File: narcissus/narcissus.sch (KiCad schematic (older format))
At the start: 71 parts, among them J1 NEIGHBOR1, J2 NEIGHBOR2, U1 PCA9698, U2 PCA9698, U3 AP2553W6-7, U4 74HC4051

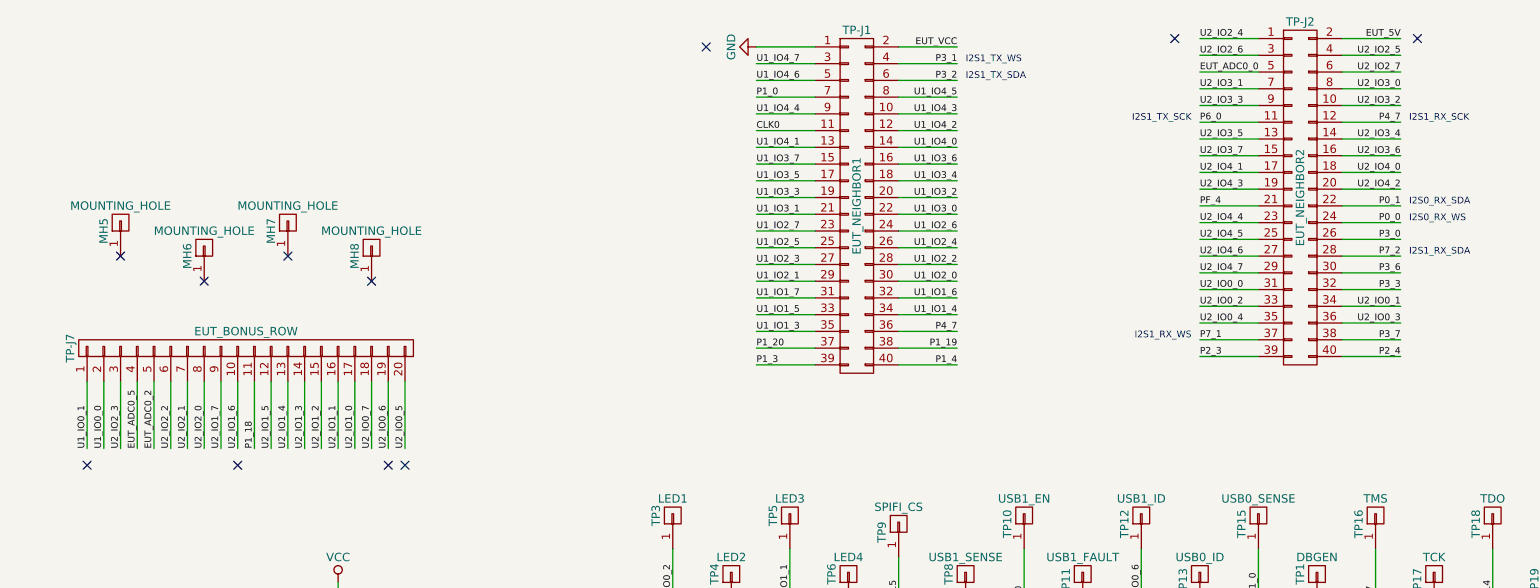
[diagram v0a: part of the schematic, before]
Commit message: Narcissus: corrected U4 pin 7 power supply connection
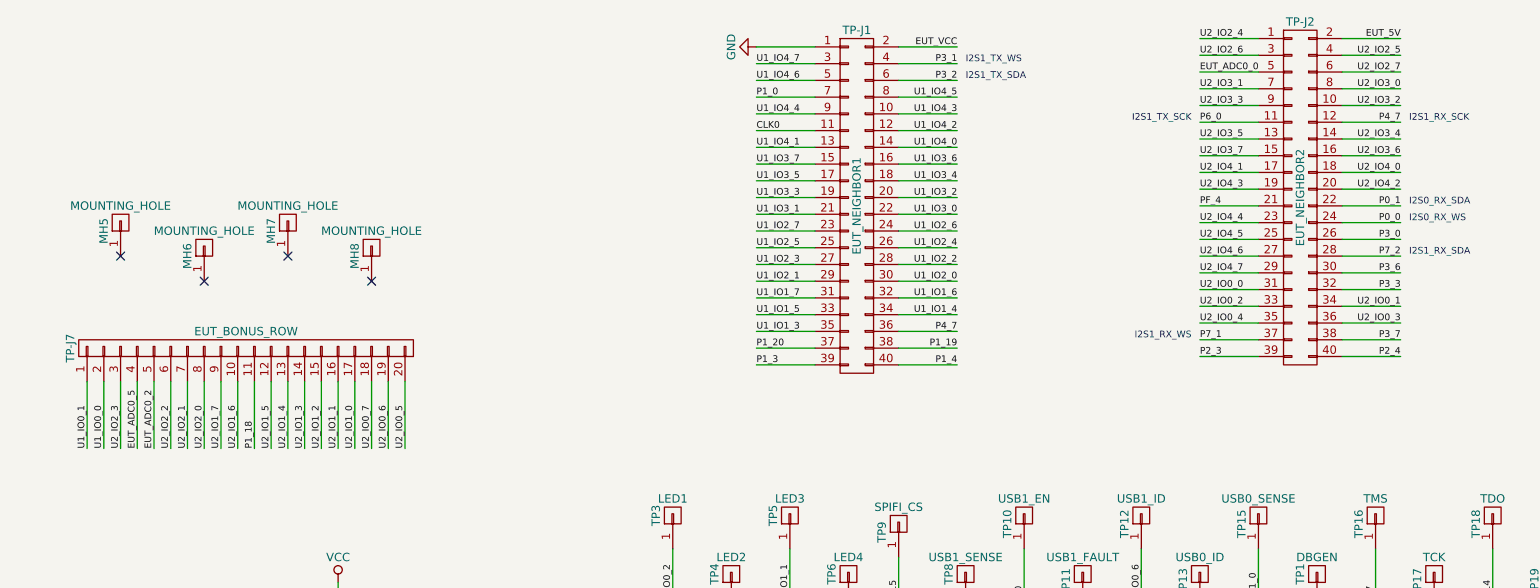
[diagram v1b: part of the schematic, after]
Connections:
- no-connect marks 48 -> 41
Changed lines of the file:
@@
 Sheet 1 1
 Title "Narcissus"
-Date "2018-06-28"
+Date "2018-07-24"
 Rev ""
 Comp "Copyright 2018 Great Scott Gadgets"
@@
 $EndComp
 $Comp
-L GND #PWR032
+L GND #PWR031
 U 1 1 5B3A7C8D
 P 3500 9300
-F 0 "#PWR032" H 3500 9050 50  0001 C CNN
+F 0 "#PWR031" H 3500 9050 50  0001 C CNN
 F 1 "GND" H 3500 9150 50  0000 C CNN
 F 2 "" H 3500 9300 50  0001 C CNN
@@
 $EndComp
 $Comp
-L VCC #PWR034
+L VCC #PWR032
 U 1 1 5B3A8A67
 P 5500 9300
-F 0 "#PWR034" H 5500 9150 50  0001 C CNN
+F 0 "#PWR032" H 5500 9150 50  0001 C CNN
 F 1 "VCC" H 5500 9450 50  0000 C CNN
 F 2 "" H 5500 9300 60  0000 C CNN
@@
 $EndComp
 $Comp
-L GND #PWR035
+L GND #PWR033
 U 1 1 5B3A8BCE
 P 5500 10000
-F 0 "#PWR035" H 5500 9750 50  0001 C CNN
+F 0 "#PWR033" H 5500 9750 50  0001 C CNN
 F 1 "GND" H 5500 9850 50  0000 C CNN
 F 2 "" H 5500 10000 50  0001 C CNN
@@
 $EndComp
 $Comp
-L VCC #PWR036
+L VCC #PWR034
 U 1 1 5B3A9F00
 P 8500 9300
-F 0 "#PWR036" H 8500 9150 50  0001 C CNN
+F 0 "#PWR034" H 8500 9150 50  0001 C CNN
 F 1 "VCC" H 8500 9450 50  0000 C CNN
 F 2 "" H 8500 9300 60  0000 C CNN
@@
 $EndComp
 $Comp
-L GND #PWR037
+L GND #PWR035
 U 1 1 5B3A9F06
 P 8500 10000
-F 0 "#PWR037" H 8500 9750 50  0001 C CNN
+F 0 "#PWR035" H 8500 9750 50  0001 C CNN
 F 1 "GND" H 8500 9850 50  0000 C CNN
 F 2 "" H 8500 10000 50  0001 C CNN
@@
 $EndComp
 $Comp
-L GND #PWR038
+L GND #PWR036
 U 1 1 5B3ACAB2
 P 1300 7850
-F 0 "#PWR038" H 1300 7600 50  0001 C CNN
+F 0 "#PWR036" H 1300 7600 50  0001 C CNN
 F 1 "GND" H 1300 7700 50  0000 C CNN
 F 2 "" H 1300 7850 50  0001 C CNN
@@
 $EndComp
 $Comp
-L GND #PWR039
+L GND #PWR037
 U 1 1 5B3AD4AC
 P 1600 7850
-F 0 "#PWR039" H 1600 7600 50  0001 C CNN
+F 0 "#PWR037" H 1600 7600 50  0001 C CNN
 F 1 "GND" H 1600 7700 50  0000 C CNN
 F 2 "" H 1600 7850 50  0001 C CNN
@@
 $EndComp
 $Comp
-L GND #PWR040
+L GND #PWR038
 U 1 1 5B3AD8B0
 P 1900 7850
-F 0 "#PWR040" H 1900 7600 50  0001 C CNN
+F 0 "#PWR038" H 1900 7600 50  0001 C CNN
 F 1 "GND" H 1900 7700 50  0000 C CNN
 F 2 "" H 1900 7850 50  0001 C CNN
@@
 $EndComp
 $Comp
-L GND #PWR041
+L GND #PWR039
 U 1 1 5B3AD8CA
 P 2200 7850
-F 0 "#PWR041" H 2200 7600 50  0001 C CNN
+F 0 "#PWR039" H 2200 7600 50  0001 C CNN
 F 1 "GND" H 2200 7700 50  0000 C CNN
 F 2 "" H 2200 7850 50  0001 C CNN
@@
 $EndComp
 $Comp
-L GND #PWR042
+L GND #PWR040
 U 1 1 5B3ADFB1
 P 2500 7850
-F 0 "#PWR042" H 2500 7600 50  0001 C CNN
+F 0 "#PWR040" H 2500 7600 50  0001 C CNN
 F 1 "GND" H 2500 7700 50  0000 C CNN
 F 2 "" H 2500 7850 50  0001 C CNN
@@
 $EndComp
 $Comp
-L GND #PWR043
+L GND #PWR041
 U 1 1 5B3B4E6D
 P 3350 5050
-F 0 "#PWR043" H 3350 4800 50  0001 C CNN
+F 0 "#PWR041" H 3350 4800 50  0001 C CNN
 F 1 "GND" H 3350 4900 50  0000 C CNN
 F 2 "" H 3350 5050 50  0001 C CNN
@@
 $EndComp
 $Comp
-L GND #PWR044
+L GND #PWR042
 U 1 1 5B3B5821
 P 1300 5050
-F 0 "#PWR044" H 1300 4800 50  0001 C CNN
+F 0 "#PWR042" H 1300 4800 50  0001 C CNN
 F 1 "GND" H 1300 4900 50  0000 C CNN
 F 2 "" H 1300 5050 50  0001 C CNN
@@
 $EndComp
 $Comp
-L GND #PWR045
+L GND #PWR043
 U 1 1 5B3B5DCA
 P 14550 2500
-F 0 "#PWR045" H 14550 2250 50  0001 C CNN
+F 0 "#PWR043" H 14550 2250 50  0001 C CNN
 F 1 "GND" H 14550 2350 50  0000 C CNN
 F 2 "" H 14550 2500 60  0000 C CNN
@@
 $EndComp
 $Comp
-L +5V #PWR046
+L +5V #PWR044
 U 1 1 5B3B625A
 P 15450 2500
-F 0 "#PWR046" H 15450 2350 50  0001 C CNN
+F 0 "#PWR044" H 15450 2350 50  0001 C CNN
 F 1 "+5V" H 15450 2640 50  0000 C CNN
 F 2 "" H 15450 2500 50  0001 C CNN
@@
 $EndComp
 $Comp
-L +5V #PWR047
+L +5V #PWR045
 U 1 1 5B3B663C
 P 1200 4550
-F 0 "#PWR047" H 1200 4400 50  0001 C CNN
+F 0 "#PWR045" H 1200 4400 50  0001 C CNN
 F 1 "+5V" H 1200 4690 50  0000 C CNN
 F 2 "" H 1200 4550 50  0001 C CNN
@@
 $EndComp
 $Comp
-L GND #PWR048
+L GND #PWR046
 U 1 1 5B3B6E27
 P 1850 4650
-F 0 "#PWR048" H 1850 4400 50  0001 C CNN
+F 0 "#PWR046" H 1850 4400 50  0001 C CNN
 F 1 "GND" H 1850 4500 50  0000 C CNN
 F 2 "" H 1850 4650 50  0001 C CNN
@@
 $EndComp
 $Comp
-L GND #PWR049
+L GND #PWR047
 U 1 1 5B3B774B
 P 1850 5250
-F 0 "#PWR049" H 1850 5000 50  0001 C CNN
+F 0 "#PWR047" H 1850 5000 50  0001 C CNN
 F 1 "GND" H 1850 5100 50  0000 C CNN
 F 2 "" H 1850 5250 50  0001 C CNN
@@
 $EndComp
 $Comp
-L VCC #PWR050
+L VCC #PWR048
 U 1 1 5B3B80DE
 P 2950 4050
-F 0 "#PWR050" H 2950 3900 50  0001 C CNN
+F 0 "#PWR048" H 2950 3900 50  0001 C CNN
 F 1 "VCC" H 2950 4200 50  0000 C CNN
 F 2 "" H 2950 4050 60  0000 C CNN
@@
 $EndComp
 $Comp
-L GND #PWR051
+L GND #PWR049
 U 1 1 5B3B8F4D
 P 2850 5250
-F 0 "#PWR051" H 2850 5000 50  0001 C CNN
+F 0 "#PWR049" H 2850 5000 50  0001 C CNN
 F 1 "GND" H 2850 5100 50  0000 C CNN
 F 2 "" H 2850 5250 50  0001 C CNN
@@
 $EndComp
 $Comp
-L VCC #PWR052
+L VCC #PWR050
 U 1 1 5B3D0463
 P 7400 8200
-F 0 "#PWR052" H 7400 8050 50  0001 C CNN
+F 0 "#PWR050" H 7400 8050 50  0001 C CNN
 F 1 "VCC" H 7400 8350 50  0000 C CNN
 F 2 "" H 7400 8200 60  0000 C CNN
@@
 $EndComp
 $Comp
-L VCC #PWR053
+L VCC #PWR051
 U 1 1 5B3D073C
 P 7150 5600
-F 0 "#PWR053" H 7150 5450 50  0001 C CNN
+F 0 "#PWR051" H 7150 5450 50  0001 C CNN
 F 1 "VCC" H 7150 5750 50  0000 C CNN
 F 2 "" H 7150 5600 60  0000 C CNN
@@
 $EndComp
 $Comp
-L VCC #PWR054
+L VCC #PWR052
 U 1 1 5B3D0B30
 P 7400 5600
-F 0 "#PWR054" H 7400 5450 50  0001 C CNN
+F 0 "#PWR052" H 7400 5450 50  0001 C CNN
 F 1 "VCC" H 7400 5750 50  0000 C CNN
 F 2 "" H 7400 5600 60  0000 C CNN
@@
 $EndComp
 $Comp
-L VCC #PWR055
+L VCC #PWR053
 U 1 1 5B3D41EC
 P 10400 8200
-F 0 "#PWR055" H 10400 8050 50  0001 C CNN
+F 0 "#PWR053" H 10400 8050 50  0001 C CNN
 F 1 "VCC" H 10400 8350 50  0000 C CNN
 F 2 "" H 10400 8200 60  0000 C CNN
@@
 $EndComp
 $Comp
-L VCC #PWR056
+L VCC #PWR054
 U 1 1 5B3D47D9
 P 10150 5600
-F 0 "#PWR056" H 10150 5450 50  0001 C CNN
+F 0 "#PWR054" H 10150 5450 50  0001 C CNN
 F 1 "VCC" H 10150 5750 50  0000 C CNN
 F 2 "" H 10150 5600 60  0000 C CNN
@@
 $EndComp
 $Comp
-L VCC #PWR057
+L VCC #PWR055
 U 1 1 5B3D47DF
 P 10400 5600
-F 0 "#PWR057" H 10400 5450 50  0001 C CNN
+F 0 "#PWR055" H 10400 5450 50  0001 C CNN
 F 1 "VCC" H 10400 5750 50  0000 C CNN
 F 2 "" H 10400 5600 60  0000 C CNN
@@
 NoConn ~ 14350 9000
 NoConn ~ 13850 8850
-NoConn ~ 1450 3350
-NoConn ~ 2350 3350
-NoConn ~ 3250 3350
-NoConn ~ 5150 850
-NoConn ~ 7950 800
-NoConn ~ 9400 800
-NoConn ~ 3350 3350
 Wire Wire Line
 	1850 9400 1950 9400

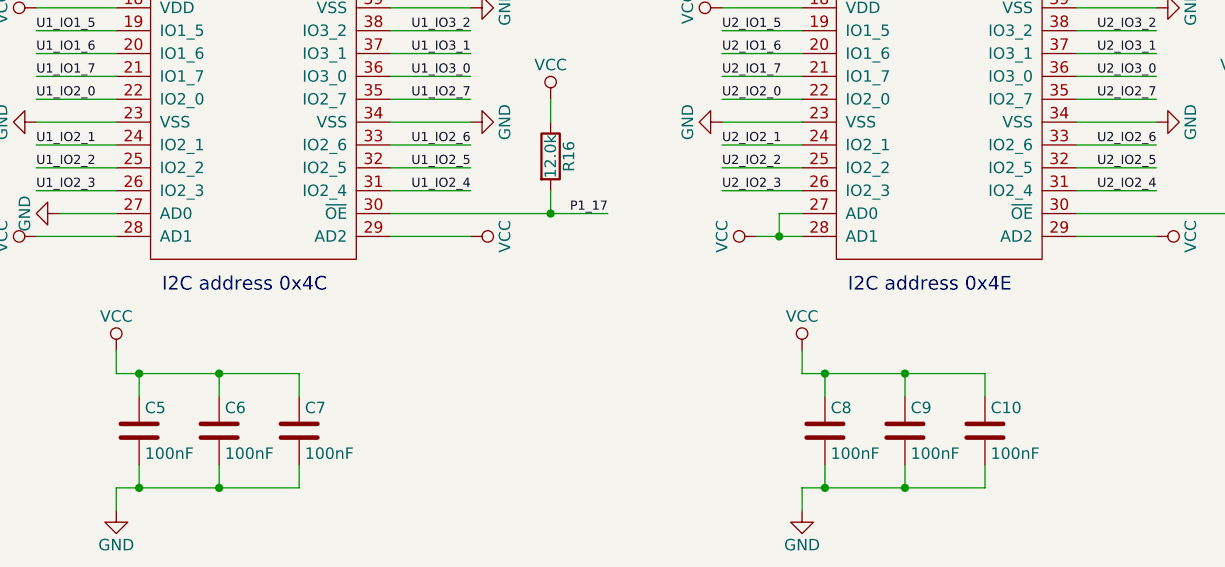
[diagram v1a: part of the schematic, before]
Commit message: standardize on 7-bit format for I2C address documentation
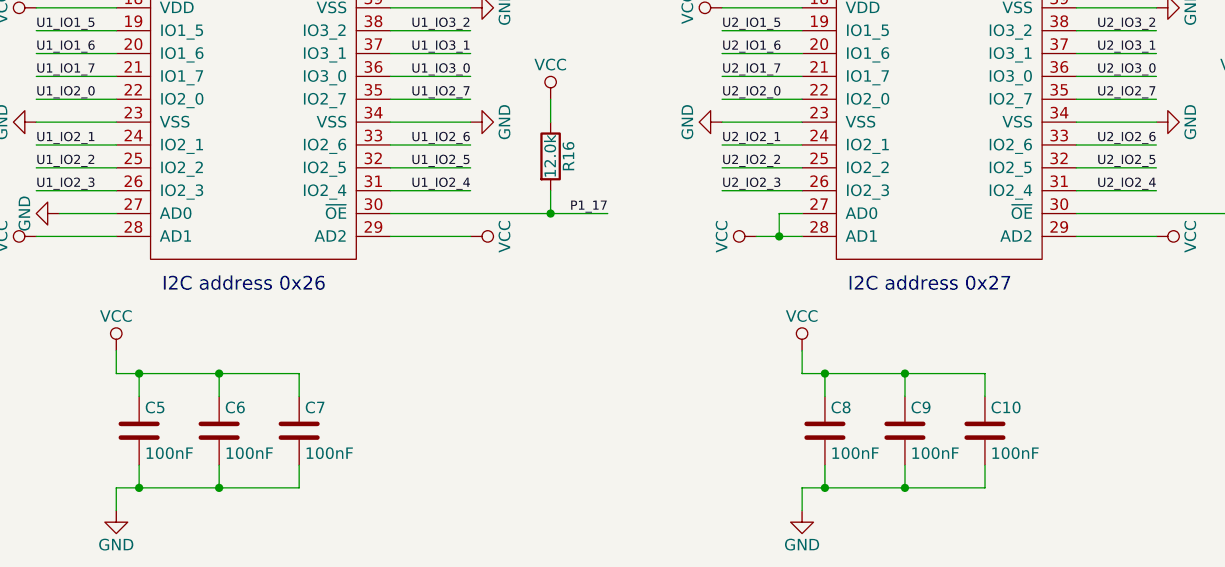
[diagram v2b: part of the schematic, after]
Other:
- note added: "I2C address 0x26"
- note added: "I2C address 0x27"
- note removed: "I2C address 0x4C"
- note removed: "I2C address 0x4E"
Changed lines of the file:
@@
 U1_IO2_1
 Text Notes 5700 9050 0    60   ~ 0
-I2C address 0x4C
+I2C address 0x26
 Text Notes 8700 9050 0    60   ~ 0
-I2C address 0x4E
+I2C address 0x27
 Text Label 6650 2150 2    40   ~ 0
 U1_IO2_2
